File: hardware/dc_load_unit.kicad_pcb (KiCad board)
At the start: 2 copper layers, 100 x 70 mm, 99 parts, among them J1 Conn_01x02_Male, J10 -V sense, J11 Conn_01x04, J12 Conn_01x03_Male, J13 Conn_02x04_Odd_Even, J14 Conn_02x05_Odd_Even, J2 Conn_01x02_Female, J3 Conn_01x02_Female, J4 Conn_01x02_Female, J5 Conn_01x02_Female, J6 Conn_01x02_Female, J7 +V sense, J8 +V, J9 -V, Q1 2N7002, Q2 2N7002, Q3 2N7002, Q4 IRFP250N, Q5 2N7002, Q6 IRFP250N, Q7 2N7002, Q8 IRFP250N, U1 DC_DC_MODULE_8_PIN, U2 LM1117-5V, U3 LM1117-5V, U4 LM358, U5 ESP32-WROOM, U6 ADS1115IDGS, U7 ACS712xLCTR-20A, U8 MCP9700, U9 MCP6241UT-E_LT

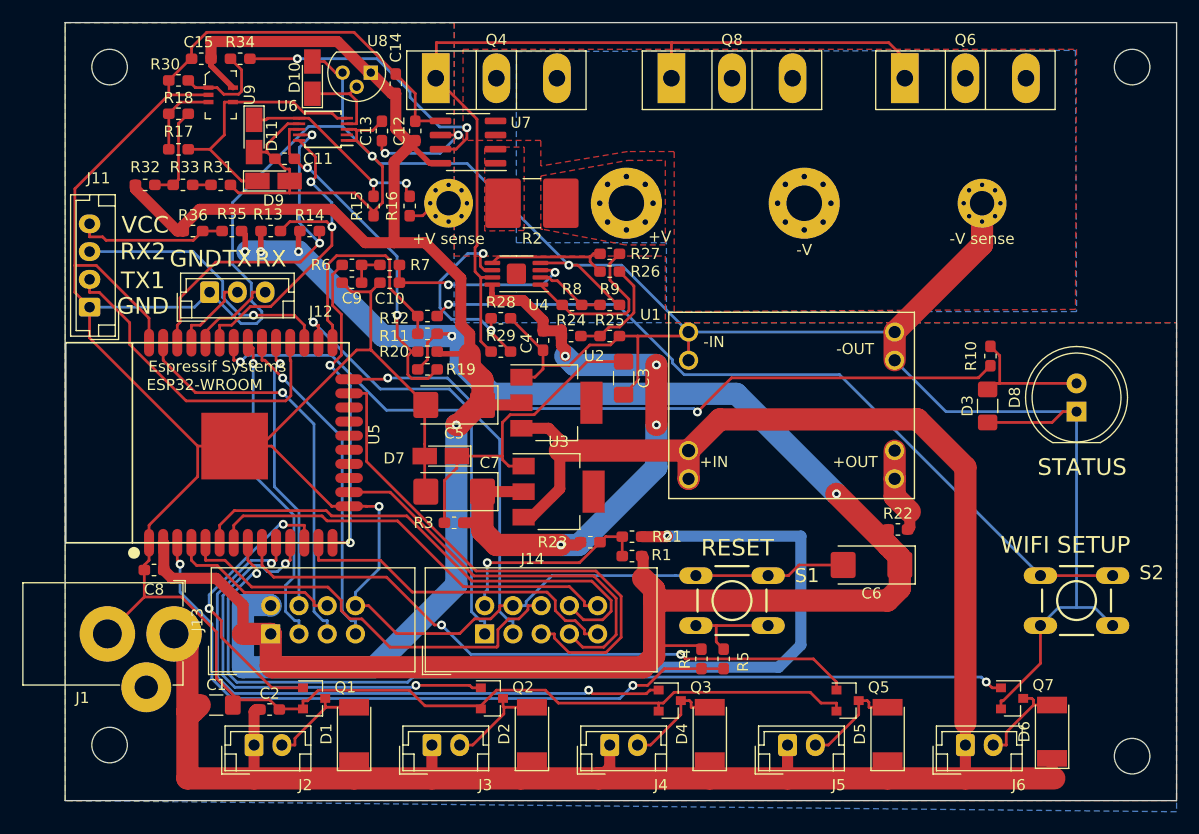
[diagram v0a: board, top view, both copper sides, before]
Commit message: Update schematic and PCB to use shunt resistors to measure throughtput and add FET protection for over current.
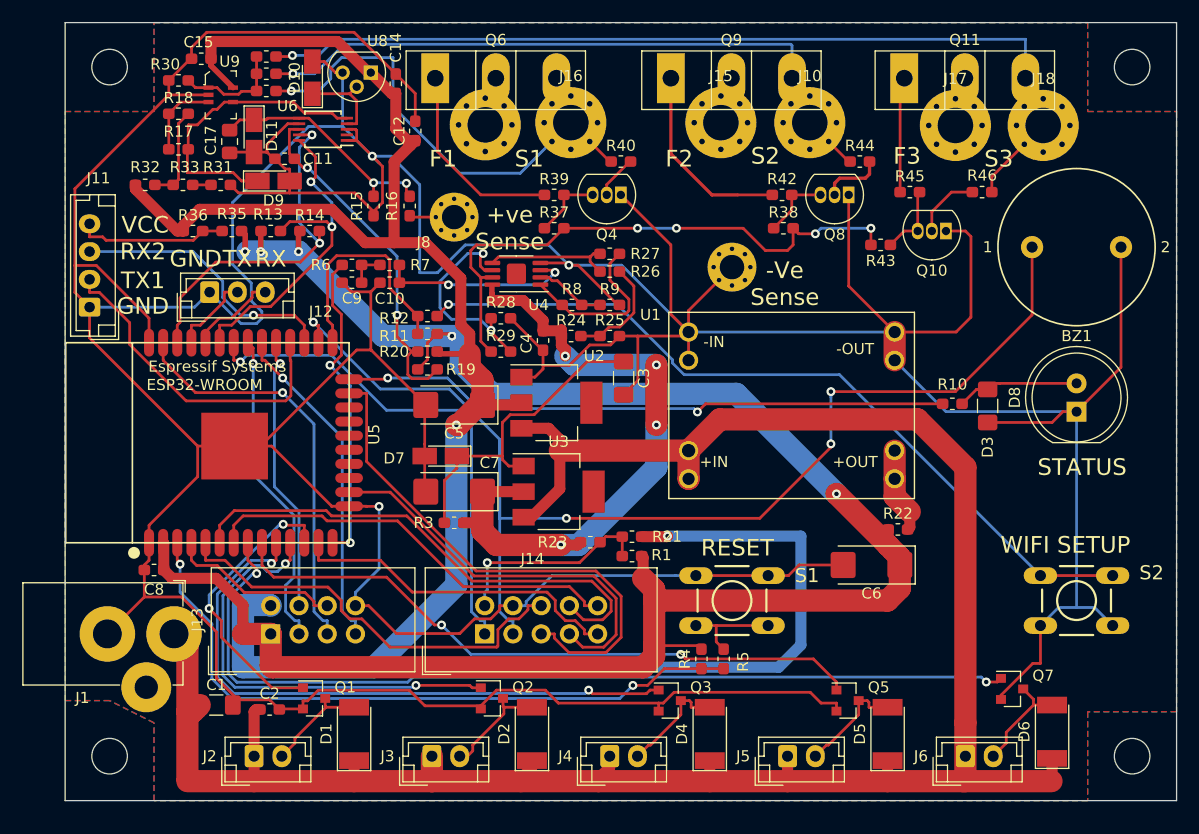
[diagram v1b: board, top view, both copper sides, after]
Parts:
- removed C13: 1nf, Capacitor_SMD:C_0603_1608Metric_Pad1.05x0.95mm_HandSolder
- removed U7: ACS712xLCTR-20A, Package_SO:SOIC-8_3.9x4.9mm_P1.27mm
- added BZ1: Buzzer, PJA_Buzzers:Buzzer_14mm_8mm_pitch, F.Cu at (191.0, 81.2)
- added C17: 470nf, Capacitor_SMD:C_0805_2012Metric_Pad1.15x1.40mm_HandSolder, F.Cu at (114.8, 71.7)
- added J15: To Fuse 2, MountingHole:MountingHole_3.2mm_M3_Pad_Via, F.Cu at (159.0, 70.0)
- added J16: 2R2 Shunt 1, MountingHole:MountingHole_3.2mm_M3_Pad_Via, F.Cu at (145.5, 70.0)
- added J17: To Fuse 3, MountingHole:MountingHole_3.2mm_M3_Pad_Via, F.Cu at (180.1, 70.2)
- added J18: 2R2 Shunt 3, MountingHole:MountingHole_3.2mm_M3_Pad_Via, F.Cu at (188.0, 70.2)
- added Q10: 2N2222, Package_TO_SOT_THT:TO-92_Inline, F.Cu at (179.2, 79.8)
- added Q11: IXFH80N25X3, Package_TO_SOT_THT:TO-247-3_Vertical, F.Cu at (175.5, 66.0)
- added Q9: IXFH80N25X3, Package_TO_SOT_THT:TO-247-3_Vertical, F.Cu at (154.5, 66.0)
- added R37: 2k2, Resistor_SMD:R_0603_1608Metric_Pad1.05x0.95mm_HandSolder, F.Cu at (144.0, 79.5)
- added R38: 2k2, Resistor_SMD:R_0603_1608Metric_Pad1.05x0.95mm_HandSolder, F.Cu at (164.6, 79.5)
- added R39: 2k2, Resistor_SMD:R_0603_1608Metric_Pad1.05x0.95mm_HandSolder, F.Cu at (144.0, 76.5)
- added R40: 39k, Resistor_SMD:R_0603_1608Metric_Pad1.05x0.95mm_HandSolder, F.Cu at (150.0, 73.5)
- added R41: 220k, Resistor_SMD:R_0603_1608Metric_Pad1.05x0.95mm_HandSolder, F.Cu at (118.1, 64.0)
- added R42: 2k2, Resistor_SMD:R_0603_1608Metric_Pad1.05x0.95mm_HandSolder, F.Cu at (164.5, 76.5)
- added R43: 2k2, Resistor_SMD:R_0603_1608Metric_Pad1.05x0.95mm_HandSolder, F.Cu at (173.4, 81.0)
- added R44: 39k, Resistor_SMD:R_0603_1608Metric_Pad1.05x0.95mm_HandSolder, F.Cu at (171.5, 73.5)
- added R45: 2k2, Resistor_SMD:R_0603_1608Metric_Pad1.05x0.95mm_HandSolder, F.Cu at (176.0, 76.2)
- added R46: 39k, Resistor_SMD:R_0603_1608Metric_Pad1.05x0.95mm_HandSolder, F.Cu at (182.5, 76.2)
- J10: value -V sense -> 2R2 Shunt 2; footprint MountingHole:MountingHole_2.2mm_M2_Pad_Via -> MountingHole:MountingHole_3.2mm_M3_Pad_Via
- J7: value +V sense -> -Ve Sense
- J8: value +V -> +Ve Sense; footprint MountingHole:MountingHole_3.2mm_M3_Pad_Via -> MountingHole:MountingHole_2.2mm_M2_Pad_Via
- J9: value -V -> To Fuse 1
- Q4, Q8: value IRFP250N -> 2N2222; footprint Package_TO_SOT_THT:TO-247-3_Vertical -> Package_TO_SOT_THT:TO-92_Inline
- Q6: value IRFP250N -> IXFH80N25X3
- R15: value 340R -> 470R
- R16: value 47k -> 33k
- R2: value 0R -> 220k; footprint Resistor_SMD:R_2816_7142Metric_Pad3.20x4.45mm_HandSolder -> Resistor_SMD:R_0603_1608Metric_Pad1.05x0.95mm_HandSolder
- R30: value 100k -> 68k
- R32: value 1k -> DNF
- R34: value 100k -> 220k
- moved Q6 42.2 mm to (133.3, 66.0)
- moved J9 29.6 mm to (137.8, 70.2)
- moved R2 26.6 mm to (118.1, 65.6), turned to 0 degrees
- moved J7 26.1 mm to (160.0, 83.0)
- moved Q4 19.7 mm to (150.0, 76.5), turned to 180 degrees
- moved Q8 19.1 mm to (170.5, 76.5), turned to 180 degrees
- moved J10 17.1 mm to (167.0, 70.0)
- moved J8 15.6 mm to (135.0, 78.5)
- moved R10 5.50 mm to (179.8, 95.3), turned to 180 degrees
- moved R34 3.73 mm to (118.1, 67.2)
- moved J2 1.00 mm to (117.0, 127.0)
- moved J3 1.00 mm to (133.0, 127.0)
- moved J4 1.00 mm to (149.0, 127.0)
- moved J5 1.00 mm to (165.0, 127.0)
- moved J6 1.00 mm to (181.0, 127.0)
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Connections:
- J10 pad 1: GND -> /High_Power/Shunt2
- J7 pad 1: Net-(J7-Pad1) -> GND
- J8 pad 1: V+ -> /High_Power/+veSense
- J9 pad 1: /FET- -> Net-(J9-Pad1)
- Q4 pad 1: /FETG -> GND
- Q4 pad 2: /FET+ -> Net-(Q4-Pad2)
- Q4 pad 3: /FET- -> Net-(Q4-Pad3)
- Q6 pad 1: /FETG -> Net-(Q6-Pad1)
- Q6 pad 2: /FET+ -> Net-(J9-Pad1)
- Q6 pad 3: /FET- -> /High_Power/Shunt1
- Q8 pad 1: /FETG -> GND
- Q8 pad 2: /FET+ -> Net-(Q8-Pad2)
- Q8 pad 3: /FET- -> Net-(Q8-Pad3)
- R16 pad 2: Net-(J7-Pad1) -> /High_Power/+veSense
- R2 pad 1: V+ -> Net-(R2-Pad1)
- R2 pad 2: IP+ -> /High_Power/Shunt2
- R29 pad 1: /FETG -> /High_Power/GateDrive
- R30 pad 1: Net-(R30-Pad1) -> Net-(R2-Pad1)
- R34 pad 1: Net-(R30-Pad1) -> Net-(R2-Pad1)
- R34 pad 2: Net-(R34-Pad2) -> /High_Power/Shunt1
- U4 pad 7: /FETG -> /High_Power/GateDrive
- U9 pad 1: Net-(R30-Pad1) -> Net-(R2-Pad1)
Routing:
- net /High_Power/Shunt3: track 0.00 -> 82.0 mm, vias 0 -> 1
- net /FETG: track 78.8 -> 0.00 mm
- net SP2: track 41.5 -> 113.1 mm, vias 1 -> 4
- net /High_Power/Shunt2: track 0.00 -> 60.3 mm, vias 0 -> 1
- net /High_Power/GateDrive: track 0.00 -> 52.2 mm, vias 0 -> 4
- net GND: track 567.7 -> 618.1 mm
- net /High_Power/Shunt1: track 0.00 -> 46.7 mm, vias 0 -> 1
- net Net-(R34-Pad2): track 26.1 -> 0.00 mm, vias 2 -> 0
- net Net-(Q6-Pad1): track 0.00 -> 18.4 mm
- net Net-(Q9-Pad1): track 0.00 -> 17.5 mm
- net Net-(J7-Pad1): track 13.0 -> 0.00 mm
- net Net-(Q11-Pad1): track 0.00 -> 10.4 mm
- net Net-(C13-Pad1): track 10.1 -> 0.00 mm, vias 2 -> 0
- net Net-(R2-Pad1): track 0.00 -> 9.89 mm
- net Net-(R30-Pad1): track 8.77 -> 0.00 mm
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- removed copper zone on F.Cu, net /FET+
- removed copper zone on B.Cu, net /FET-
- removed copper zone on F.Cu, net IP+
- removed copper zone on F.Cu, net V+
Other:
- board text added: "+ve Sense"
- board text added: "-Ve Sense"
- board text added: "F1"
- board text added: "F2"
- board text added: "F3"
- board text added: "S1"
- board text added: "S2"
- board text added: "S3"

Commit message: R10 330R -> 681R as LED is too bright R25 3.3k -> 2.2k to change low end gate voltage
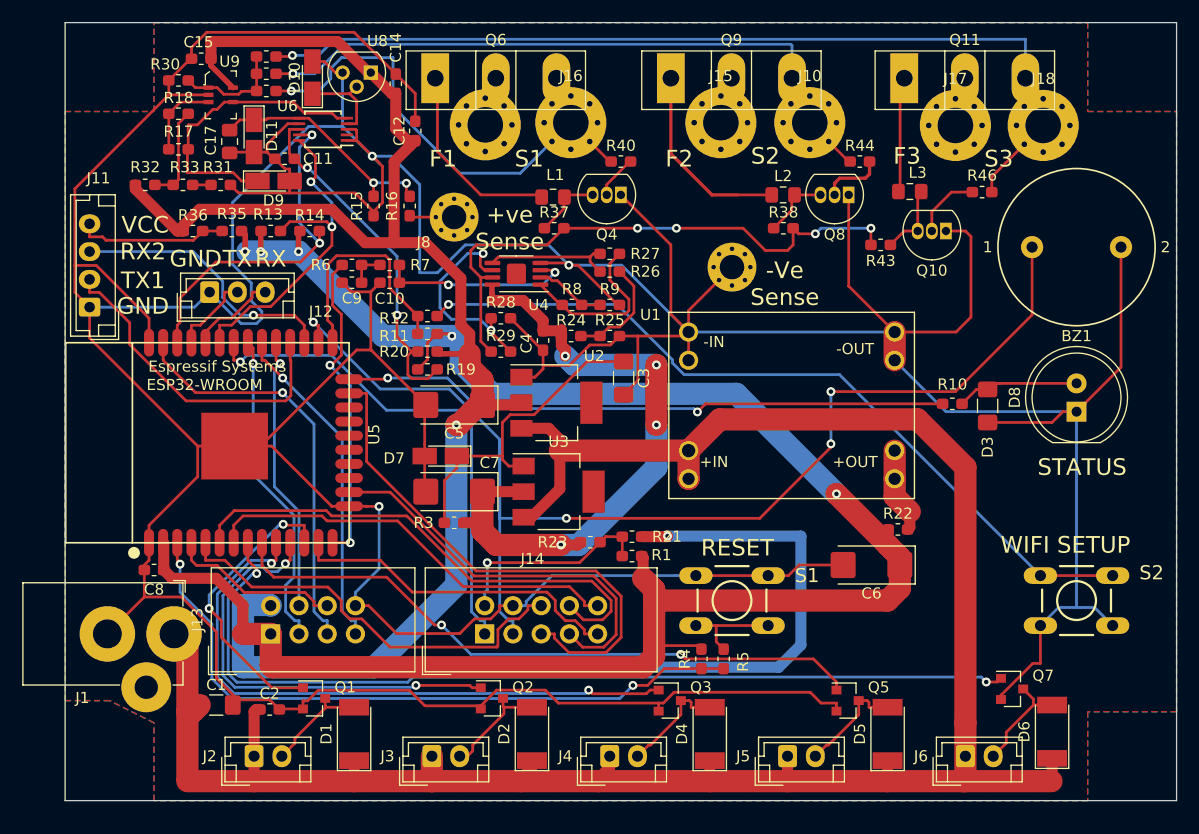
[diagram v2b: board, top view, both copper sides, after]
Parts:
- removed MH1, MH2, MH3, MH4: MountingHole_3.2mm_M3, MountingHole:MountingHole_3.2mm_M3
- removed R39, R42, R45: 2k2, Resistor_SMD:R_0603_1608Metric_Pad1.05x0.95mm_HandSolder
- added L1: 2.2uh, Inductor_SMD:L_0805_2012Metric_Pad1.15x1.40mm_HandSolder, F.Cu at (143.9, 76.7)
- added L2: 2.2uh, Inductor_SMD:L_0805_2012Metric_Pad1.15x1.40mm_HandSolder, F.Cu at (164.6, 76.5)
- added L3: 2.2uh, Inductor_SMD:L_0805_2012Metric_Pad1.15x1.40mm_HandSolder, F.Cu at (176.0, 76.2)
- J10: value 2R2 Shunt 2 -> 0.1R Shunt 2
- J16: value 2R2 Shunt 1 -> 0.1R Shunt 1
- J18: value 2R2 Shunt 3 -> 0.1R Shunt 3
- R10: value 330R -> 681R
- R25: value 3.3k -> 2.2k
- R40, R44, R46: value 39k -> 220k
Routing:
- net Net-(L1-Pad2): track 18.4 -> 17.7 mm

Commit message: Rev 1.3 single shunt with op amp drive change to make gate drive voltage directly related to load current.
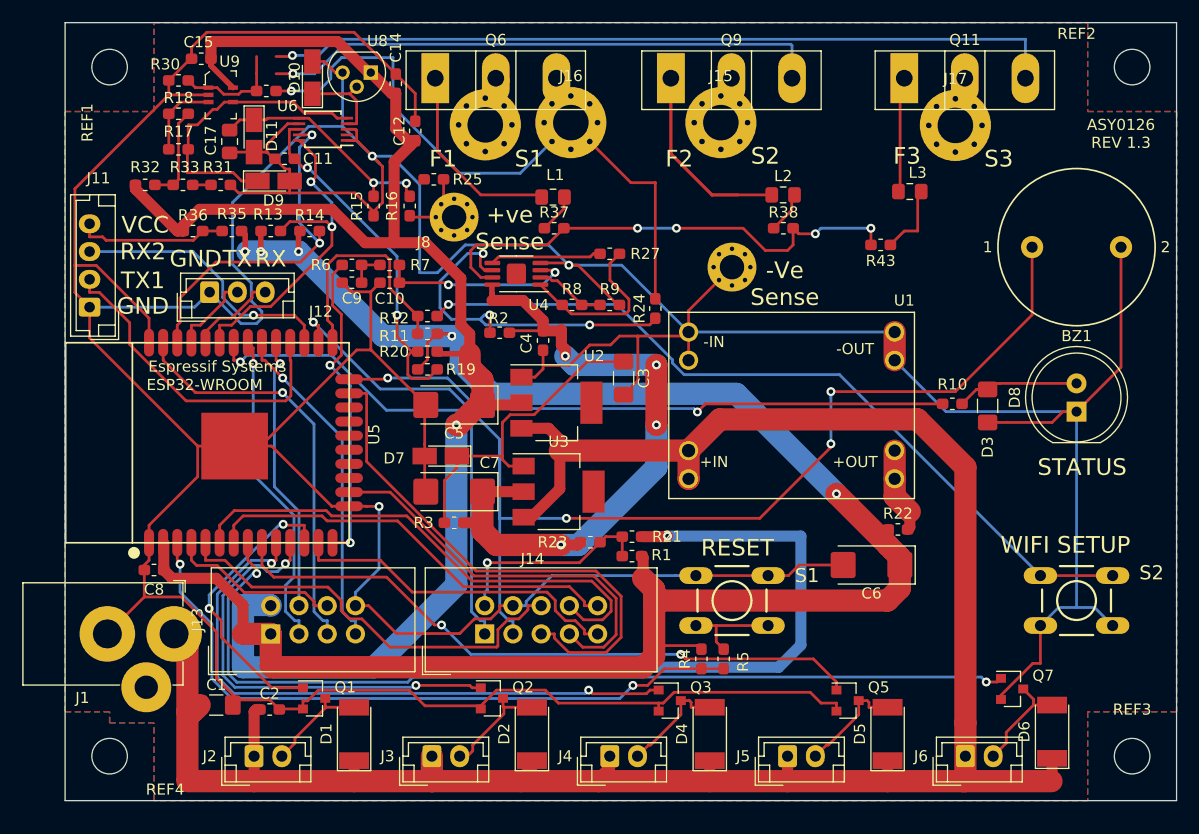
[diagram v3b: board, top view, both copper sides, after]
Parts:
- removed J10: 0.1R Shunt 2, MountingHole:MountingHole_3.2mm_M3_Pad_Via
- removed J18: 0.1R Shunt 3, MountingHole:MountingHole_3.2mm_M3_Pad_Via
- removed Q10, Q4, Q8: 2N2222, Package_TO_SOT_THT:TO-92_Inline
- removed R26: 47k, Resistor_SMD:R_0603_1608Metric_Pad1.05x0.95mm_HandSolder
- removed R28, R29: 10k, Resistor_SMD:R_0603_1608Metric_Pad1.05x0.95mm_HandSolder
- removed R40, R41, R44, R46: 220k, Resistor_SMD:R_0603_1608Metric_Pad1.05x0.95mm_HandSolder
- added REF1: MountingHole_3.2mm_M3, MountingHole:MountingHole_3.2mm_M3, F.Cu at (104.0, 65.0)
- added REF2: MountingHole_3.2mm_M3, MountingHole:MountingHole_3.2mm_M3, F.Cu at (196.0, 65.0)
- added REF3: MountingHole_3.2mm_M3, MountingHole:MountingHole_3.2mm_M3, F.Cu at (196.0, 127.0)
- added REF4: MountingHole_3.2mm_M3, MountingHole:MountingHole_3.2mm_M3, F.Cu at (104.0, 127.0)
- J16: value 0.1R Shunt 1 -> 0.22R Shunt
- R2: value 220k -> 150k
- R24: value 6.8k -> 100R
- R25: value 2.2k -> 100k
- R27: value 47k -> 0R
- R34: value 220k -> 33k
- moved R2 31.4 mm to (139.1, 88.9), turned to 180 degrees
- moved R25 21.2 mm to (133.2, 75.1), turned to 180 degrees
- moved R24 7.97 mm to (153.1, 86.7), turned to 90 degrees
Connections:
- J16 pad 1: /High_Power/Shunt1 -> /High_Power/Shunt
- Q11 pad 3: /High_Power/Shunt3 -> /High_Power/Shunt
- Q6 pad 3: /High_Power/Shunt1 -> /High_Power/Shunt
- Q9 pad 3: /High_Power/Shunt2 -> /High_Power/Shunt
- R2 pad 1: Net-(R2-Pad1) -> 9V7
- R2 pad 2: /High_Power/Shunt2 -> Net-(R2-Pad2)
- R24 pad 1: 9V7 -> Net-(R2-Pad2)
- R24 pad 2: Net-(R24-Pad2) -> /High_Power/Shunt
- R25 pad 1: Net-(R24-Pad2) -> /High_Power/+veSense
- R30 pad 1: Net-(R2-Pad1) -> Net-(R30-Pad1)
- R34 pad 1: Net-(R2-Pad1) -> Net-(R30-Pad1)
- R34 pad 2: /High_Power/Shunt1 -> /High_Power/Shunt
- U4 pad 6: Net-(R28-Pad1) -> Net-(R2-Pad2)
- U5 pad 17: Net-(U5-Pad17) -> (no net)
- U5 pad 18: Net-(U5-Pad18) -> (no net)
- U5 pad 19: Net-(U5-Pad19) -> (no net)
- U5 pad 20: Net-(U5-Pad20) -> (no net)
- U5 pad 21: Net-(U5-Pad21) -> (no net)
- U5 pad 22: Net-(U5-Pad22) -> (no net)
- U6 pad 2: Net-(U6-Pad2) -> (no net)
- U9 pad 1: Net-(R2-Pad1) -> Net-(R30-Pad1)
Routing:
- net /High_Power/Shunt: track 0.00 -> 184.0 mm, vias 0 -> 3
- net /High_Power/Shunt3: track 82.0 -> 0.00 mm, vias 1 -> 0
- net /High_Power/Shunt2: track 60.3 -> 0.00 mm, vias 1 -> 0
- net GND: track 618.1 -> 568.0 mm
- net /High_Power/Shunt1: track 46.7 -> 0.00 mm, vias 1 -> 0
- net Net-(R2-Pad2): track 0.00 -> 32.7 mm, vias 0 -> 3
- net Net-(R28-Pad1): track 18.9 -> 0.00 mm, vias 2 -> 0
- net Net-(R24-Pad2): track 9.89 -> 0.00 mm
- net Net-(R30-Pad1): track 0.00 -> 9.89 mm
- net Net-(R2-Pad1): track 9.89 -> 0.00 mm
- net /High_Power/GateDrive: track 52.2 -> 45.1 mm
- net Net-(Q10-Pad2): track 6.11 -> 0.00 mm
- net Net-(Q8-Pad2): track 5.66 -> 0.00 mm
- net Net-(Q4-Pad2): track 4.26 -> 0.00 mm
- net /High_Power/+veSense: track 4.05 -> 7.85 mm
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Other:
- board text added: "ASY0126 REV 1.3"
